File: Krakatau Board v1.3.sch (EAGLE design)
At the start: 139 parts, among them J1 MMCX-P-P-X-ST-TH1, J12 SAMTEC-CLP-110-02-X-D, J2 MMCX-P-P-X-ST-TH1, J8 61300511121, SW1 TL3342F160QG, T1 SUM110P06-07L-E3, U1 STM32F413VHT6, U10 TESEO-LIV3F, U11 BGA725L6E6327FTSA1, U12 DS3231S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

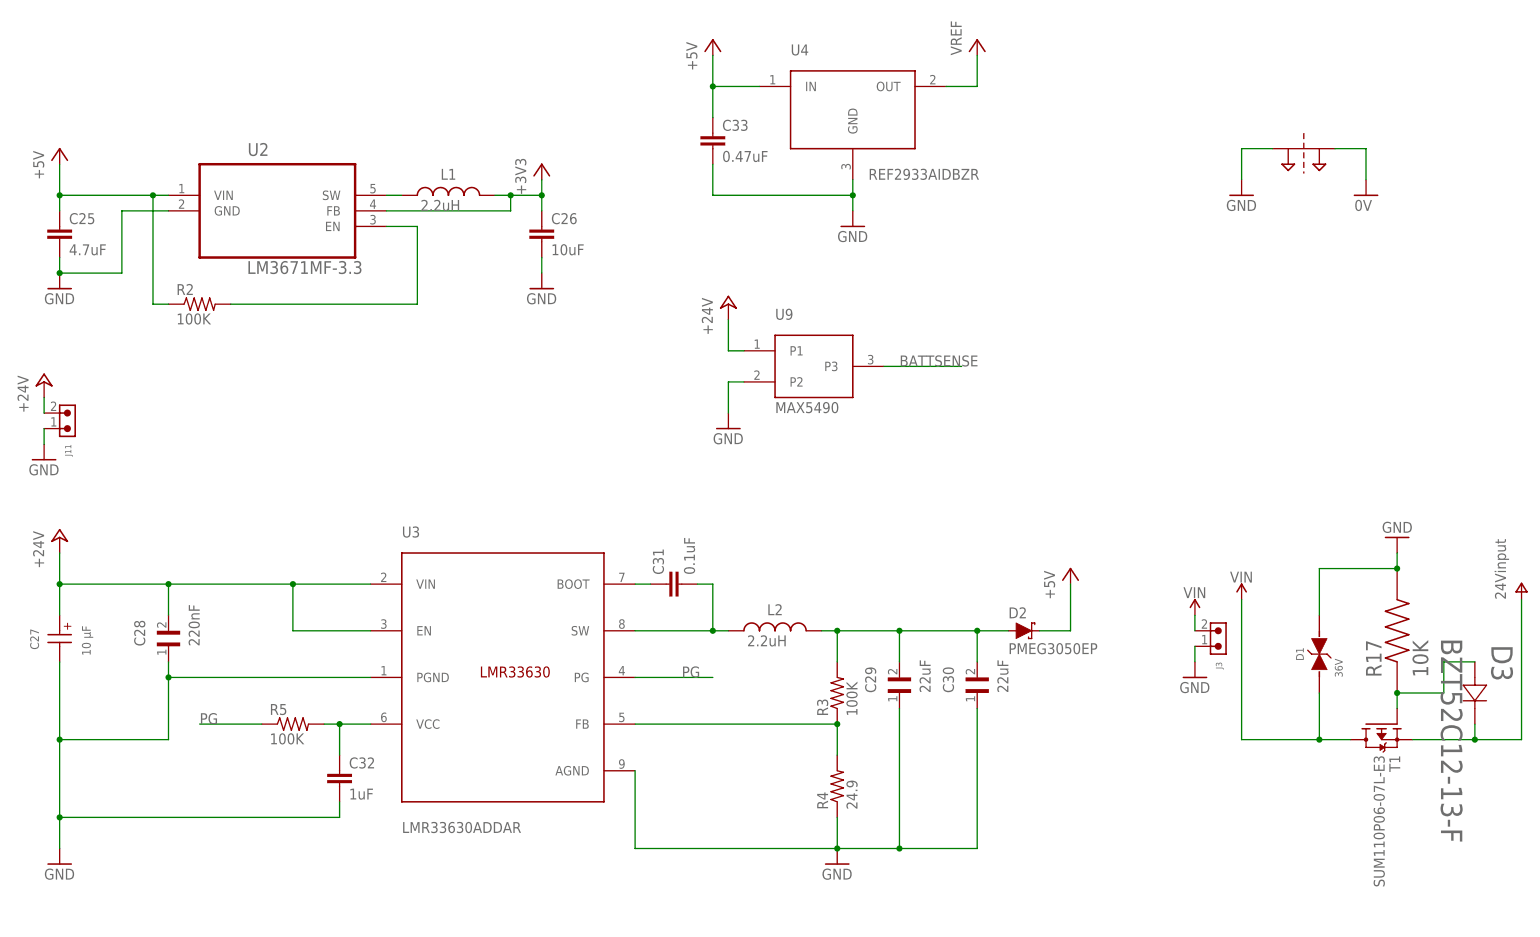
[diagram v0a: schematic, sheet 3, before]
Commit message: vias 0.25 min pcbway for 2mm
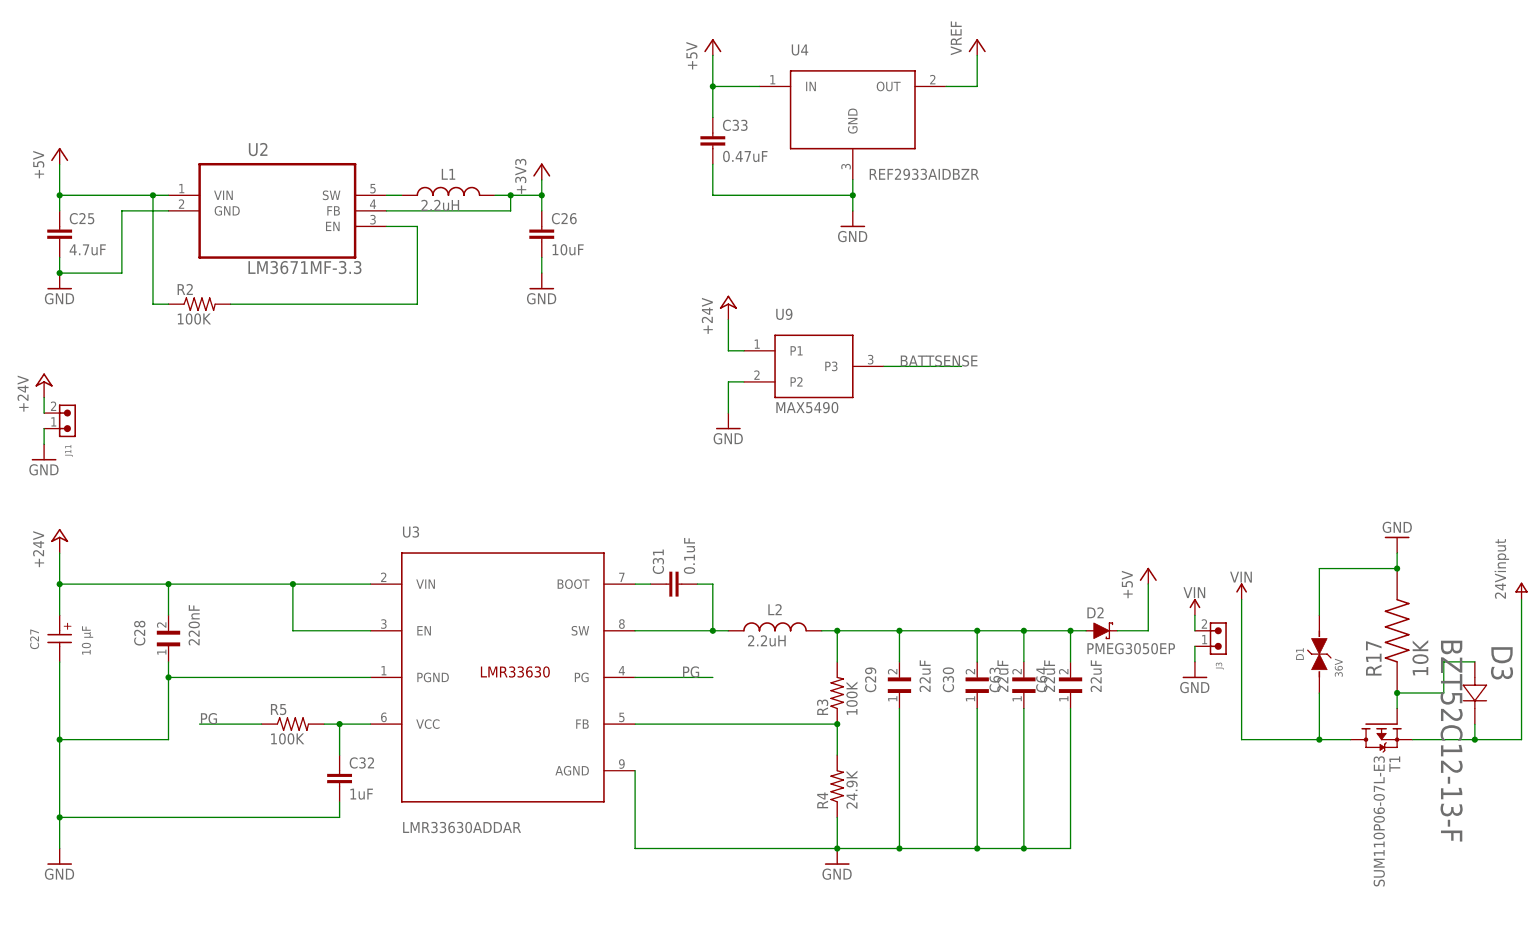
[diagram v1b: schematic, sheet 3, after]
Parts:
- removed SUPPLY3: 2PT_GND_TIE, SparkFun-PowerSymbols:2PT_GND_TIE
- added C63, C64: 22uF, LMK212BBJ226MD-T:LMK212BBJ226MD-T
- added J15: 61300311121, Headers:61300311121
- R4: value 24.9 -> 24.9K
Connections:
- removed net 0V: SUPPLY3.P$2, U14.ADIN, U14.ADR0, U14.GND
- net BT_CLK: now also J15.2
- net BT_DIO: now also J15.1
- net BT_RESET: now also J15.3
- net GND: now also C63.1, C64.1, U14.ADIN, U14.ADR0, U14.GND; no longer SUPPLY3.P$1
- net N$12: now also C63.2, C64.2
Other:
- moved on the sheet: D2
